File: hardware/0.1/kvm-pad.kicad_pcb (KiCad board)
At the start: 2 copper layers, 53 parts, among them J1 USB_C_Receptacle_USB2.0, J2 USB_C_Receptacle_USB2.0, J3 USB_A, J4 USB_A, J5 USB_A, U1 USBLC6-2SC6, U2 USBLC6-2SC6, U3 TS3USB30, U4 TPS211x, U5 CY7C65632-28LTXCT, Y1 12MHz

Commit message: update mask gap to 50 um
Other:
- rule pad_to_mask_clearance: 0 -> 0.05

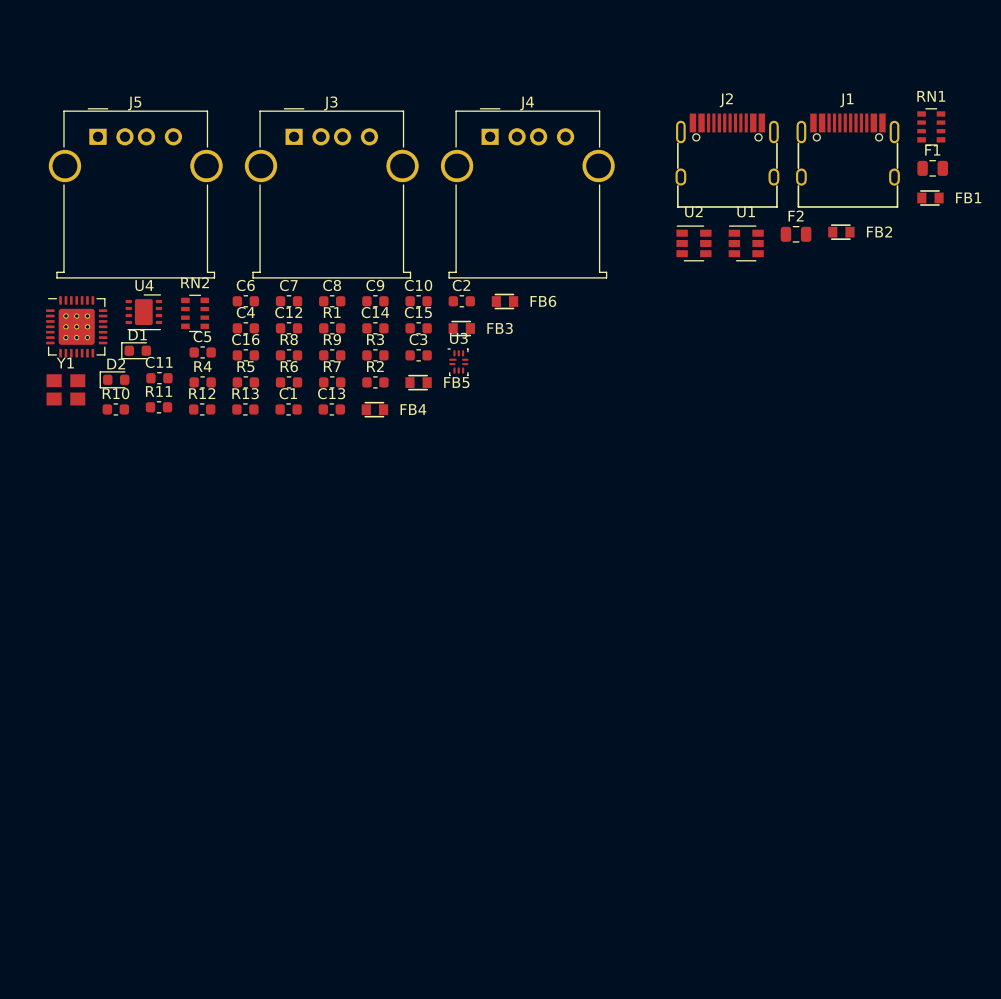
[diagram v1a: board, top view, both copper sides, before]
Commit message: Update jkl & footprints
USBA / Kailh Choc / ATMEGA32U4-AU
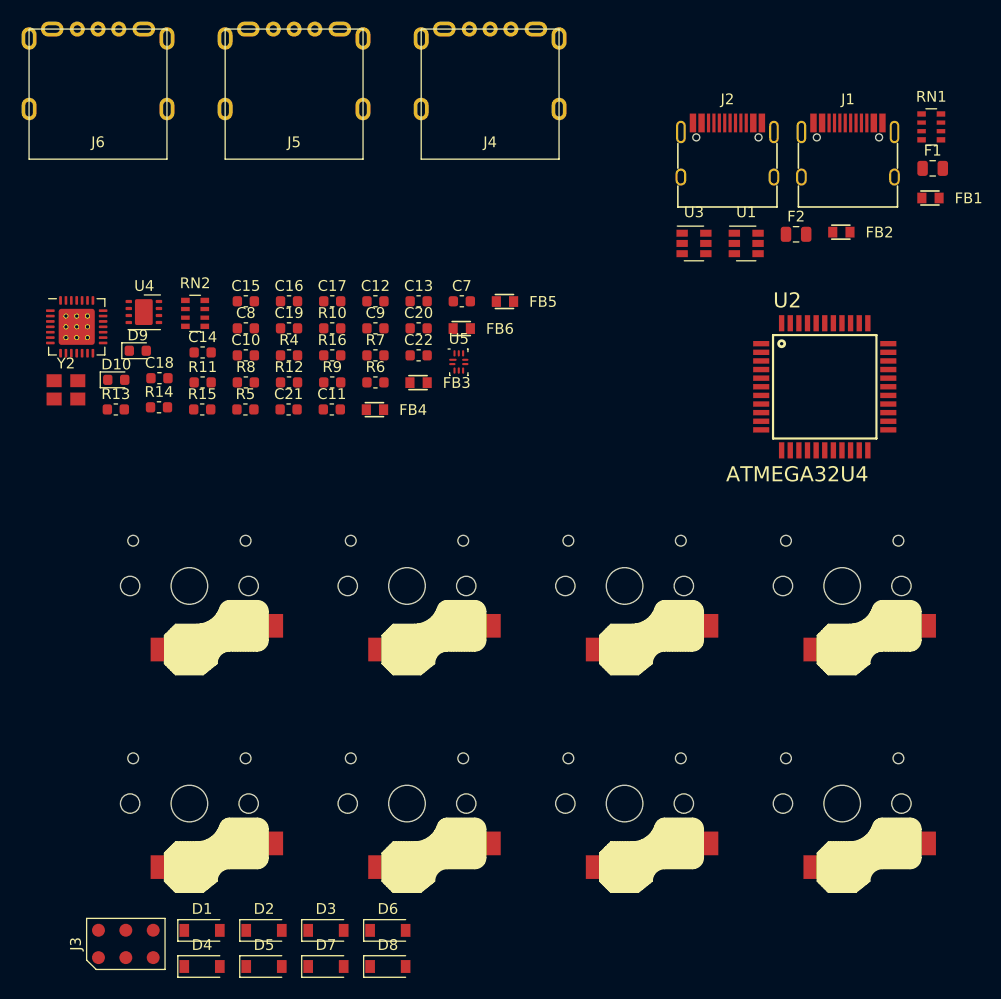
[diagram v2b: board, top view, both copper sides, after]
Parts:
- added D1: D, Diode_SMD:D_SOD-123, F.Cu at (32.4, 94.7)
- added D2: D, Diode_SMD:D_SOD-123, F.Cu at (38.1, 94.7)
- added D3: D, Diode_SMD:D_SOD-123, F.Cu at (43.9, 94.7)
- added D4: D, Diode_SMD:D_SOD-123, F.Cu at (32.4, 98.0)
- added D5: D, Diode_SMD:D_SOD-123, F.Cu at (38.1, 98.0)
- added D6: D, Diode_SMD:D_SOD-123, F.Cu at (49.6, 94.7)
- added D7: D, Diode_SMD:D_SOD-123, F.Cu at (43.9, 98.0)
- added D8: D, Diode_SMD:D_SOD-123, F.Cu at (49.6, 98.0)
- added J6: USB_A, josh-connectors:USB_A_U234-051N-3GRA035-5, F.Cu at (22.7, 21.0)
- added K1: KEYSW, josh-keyboard:Choc_Hotswap, F.Cu at (31.2, 62.7)
- added K2: KEYSW, josh-keyboard:Choc_Hotswap, F.Cu at (31.2, 82.9)
- added K3: KEYSW, josh-keyboard:Choc_Hotswap, F.Cu at (51.4, 62.7)
- added K4: KEYSW, josh-keyboard:Choc_Hotswap, F.Cu at (51.4, 82.9)
- added K5: KEYSW, josh-keyboard:Choc_Hotswap, F.Cu at (71.6, 62.7)
- added K6: KEYSW, josh-keyboard:Choc_Hotswap, F.Cu at (71.6, 82.9)
- added K7: KEYSW, josh-keyboard:Choc_Hotswap, F.Cu at (91.8, 62.7)
- added K8: KEYSW, josh-keyboard:Choc_Hotswap, F.Cu at (91.8, 82.9)
- added U2: ATMEGA32U4, josh-dfn-qfn:ATMEGA32U4-AU, F.Cu at (90.2, 44.2)
- J3: value USB_A -> AVR-ISP-6; footprint josh-connectors:USB_A_Molex_67643_Horizontal -> josh-connectors:AVR_PROG_2.54_SMT
- J4, J5: footprint josh-connectors:USB_A_Molex_67643_Horizontal -> josh-connectors:USB_A_U234-051N-3GRA035-5
- moved J3 76.5 mm to (25.3, 95.9)
- moved J5 18.2 mm to (40.9, 21.0)
- renumbered C16 to C10, C13 to C11, C9 to C12, C10 to C13, C5 to C14, C6 to C15, C7 to C16, C8 to C17, C11 to C18, C12 to C19, C15 to C20, C1 to C21, C3 to C22, C2 to C7, C4 to C8, C14 to C9, D2 to D10, D1 to D9, FB5 to FB3, FB6 to FB5, FB3 to FB6, R1 to R10, R4 to R11, R6 to R12, R10 to R13, R11 to R14, R12 to R15, R9 to R16, R8 to R4, R13 to R5, R2 to R6, R3 to R7, R5 to R8, R7 to R9, U2 to U3, U3 to U5, U5 to U6, Y1 to Y2
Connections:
- FB5 pad 1: Net-(FB6-Pad1) -> Net-(FB5-Pad1)
- J1 pad A8: (no net) -> Net-(J1-PadA8)
- J1 pad B8: (no net) -> Net-(J1-PadB8)
- J2 pad A8: (no net) -> Net-(J2-PadA8)
- J2 pad B8: (no net) -> Net-(J2-PadB8)
- J3 pad 1: Net-(FB4-Pad1) -> /MISO
- J3 pad 2: /usb/D2_D- -> +5V
- J3 pad 3: /usb/D2_D+ -> /SCK
- J3 pad 4: GND -> /MOSI
- J3 pad 5: GND -> /nRST
- J5 pad 1: Net-(FB6-Pad1) -> Net-(FB4-Pad1)
- J5 pad 2: /usb/D3_D- -> /usb/D2_D-
- J5 pad 3: /usb/D3_D+ -> /usb/D2_D+
- R10 pad 2: (no net) -> /SWITCH
- U6 pad 15: (no net) -> /MCU_D-
- U6 pad 16: (no net) -> /MCU_D+
- U6 pad 18: (no net) -> Net-(U6-Pad18)
- U6 pad 26: (no net) -> Net-(U6-Pad26)

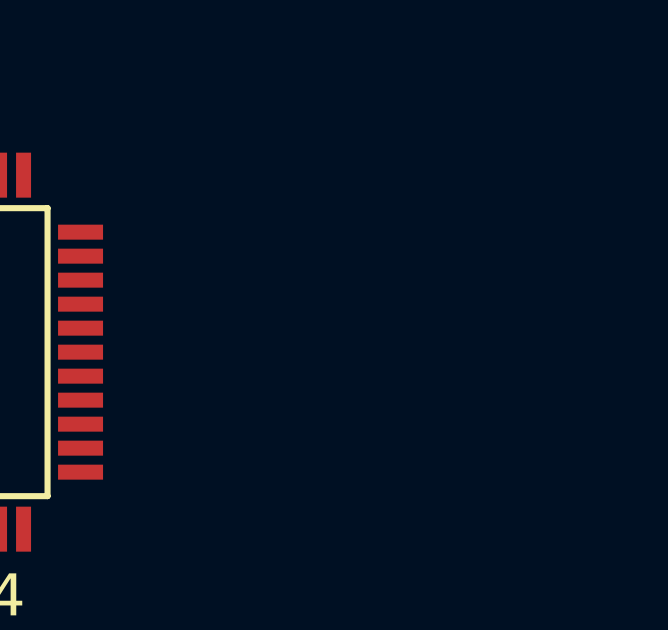
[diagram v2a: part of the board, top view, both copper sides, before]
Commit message: Add missing footprints
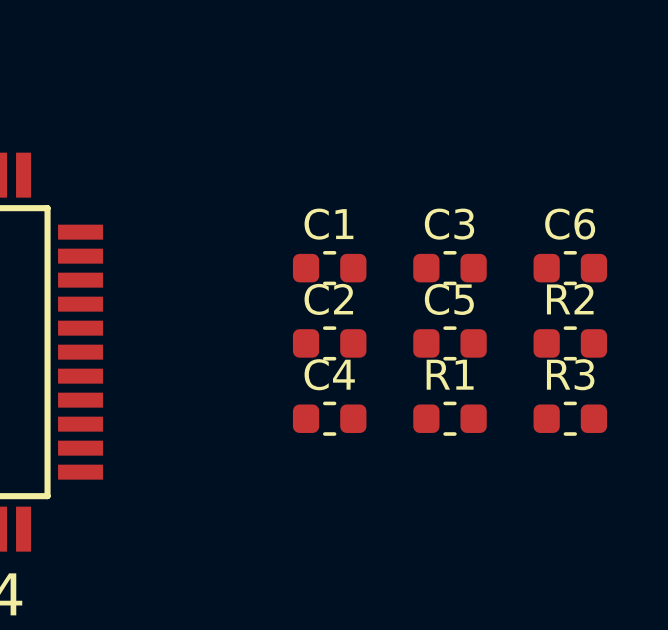
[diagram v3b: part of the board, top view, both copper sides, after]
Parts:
- added C1: 1u, Capacitor_SMD:C_0603_1608Metric, F.Cu at (104.4, 41.4)
- added C2: 100n, Capacitor_SMD:C_0603_1608Metric, F.Cu at (104.4, 43.9)
- added C3: 100n, Capacitor_SMD:C_0603_1608Metric, F.Cu at (108.4, 41.4)
- added C4: 22p, Capacitor_SMD:C_0603_1608Metric, F.Cu at (104.4, 46.4)
- added C5: 22p, Capacitor_SMD:C_0603_1608Metric, F.Cu at (108.4, 43.9)
- added C6: 1u, Capacitor_SMD:C_0603_1608Metric, F.Cu at (112.4, 41.4)
- added R1: 22R, Resistor_SMD:R_0603_1608Metric, F.Cu at (108.4, 46.4)
- added R2: 22R, Resistor_SMD:R_0603_1608Metric, F.Cu at (112.4, 43.9)
- added R3: 10K, Resistor_SMD:R_0603_1608Metric, F.Cu at (112.4, 46.4)

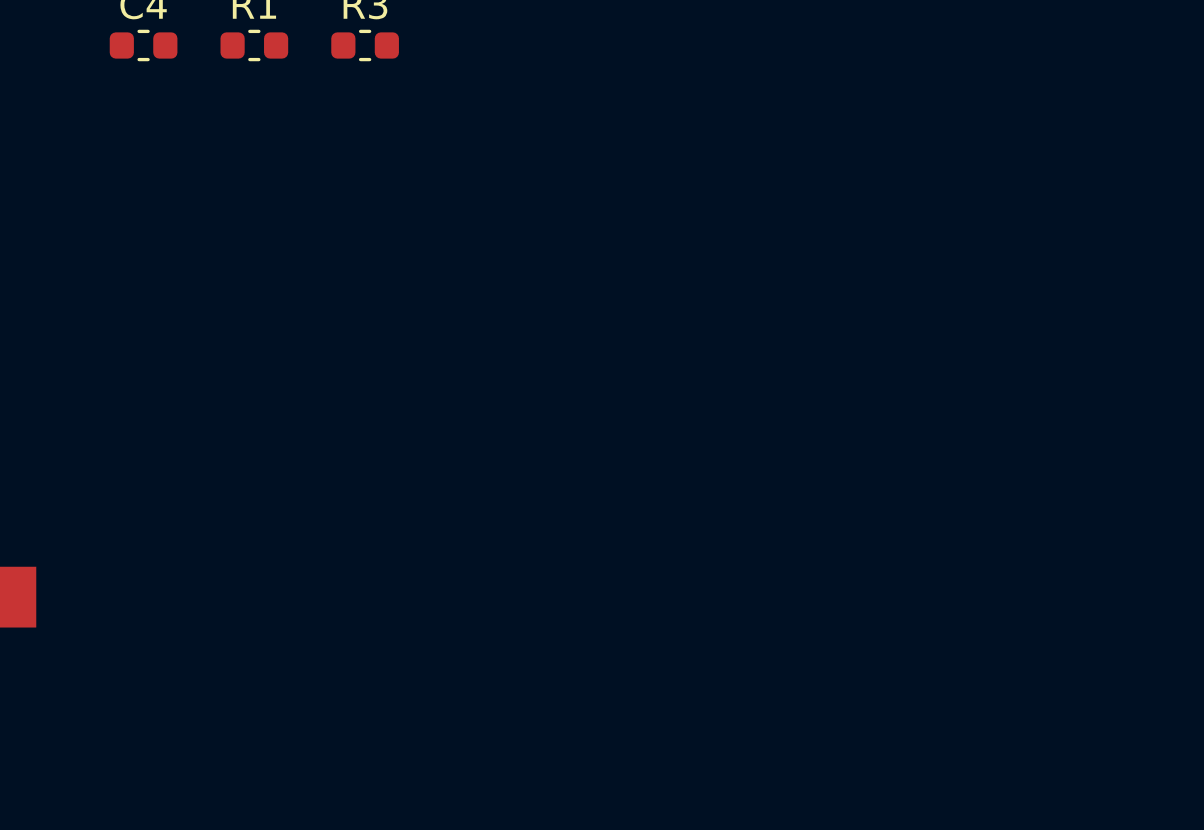
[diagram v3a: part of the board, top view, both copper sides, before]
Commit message: Add RGB LEDs
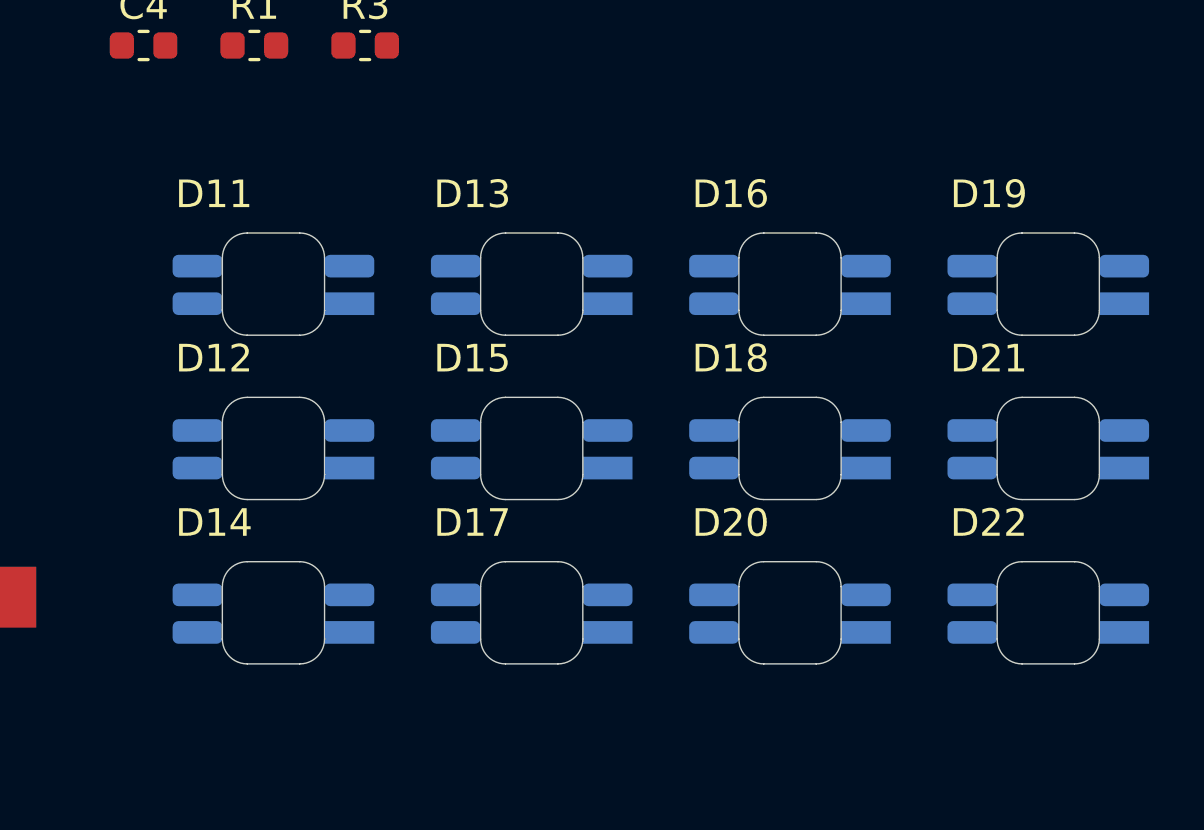
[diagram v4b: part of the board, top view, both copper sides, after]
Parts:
- added D11: WS2812B, josh-led:SK8612-MINI-E, F.Cu at (109.0, 55.1)
- added D12: WS2812B, josh-led:SK8612-MINI-E, F.Cu at (109.0, 61.1)
- added D13: WS2812B, josh-led:SK8612-MINI-E, F.Cu at (118.4, 55.1)
- added D14: WS2812B, josh-led:SK8612-MINI-E, F.Cu at (109.0, 67.0)
- added D15: WS2812B, josh-led:SK8612-MINI-E, F.Cu at (118.4, 61.1)
- added D16: WS2812B, josh-led:SK8612-MINI-E, F.Cu at (127.7, 55.1)
- added D17: WS2812B, josh-led:SK8612-MINI-E, F.Cu at (118.4, 67.0)
- added D18: WS2812B, josh-led:SK8612-MINI-E, F.Cu at (127.7, 61.1)
- added D19: WS2812B, josh-led:SK8612-MINI-E, F.Cu at (137.1, 55.1)
- added D20: WS2812B, josh-led:SK8612-MINI-E, F.Cu at (127.7, 67.0)
- added D21: WS2812B, josh-led:SK8612-MINI-E, F.Cu at (137.1, 61.1)
- added D22: WS2812B, josh-led:SK8612-MINI-E, F.Cu at (137.1, 67.0)
- moved LOGO1 108.0 mm to (102.9, 100.6)
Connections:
- U2 pad 18: /col1 -> Net-(U2-Pad18)
- U2 pad 19: /col2 -> /LED_DAT
- U2 pad 20: /col3 -> /col1
- U2 pad 21: /col4 -> /col2
- U2 pad 22: Net-(U2-Pad22) -> /col4
- U2 pad 25: Net-(U2-Pad25) -> /col3
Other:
- board outline added: 3.7 x 3.7 mm

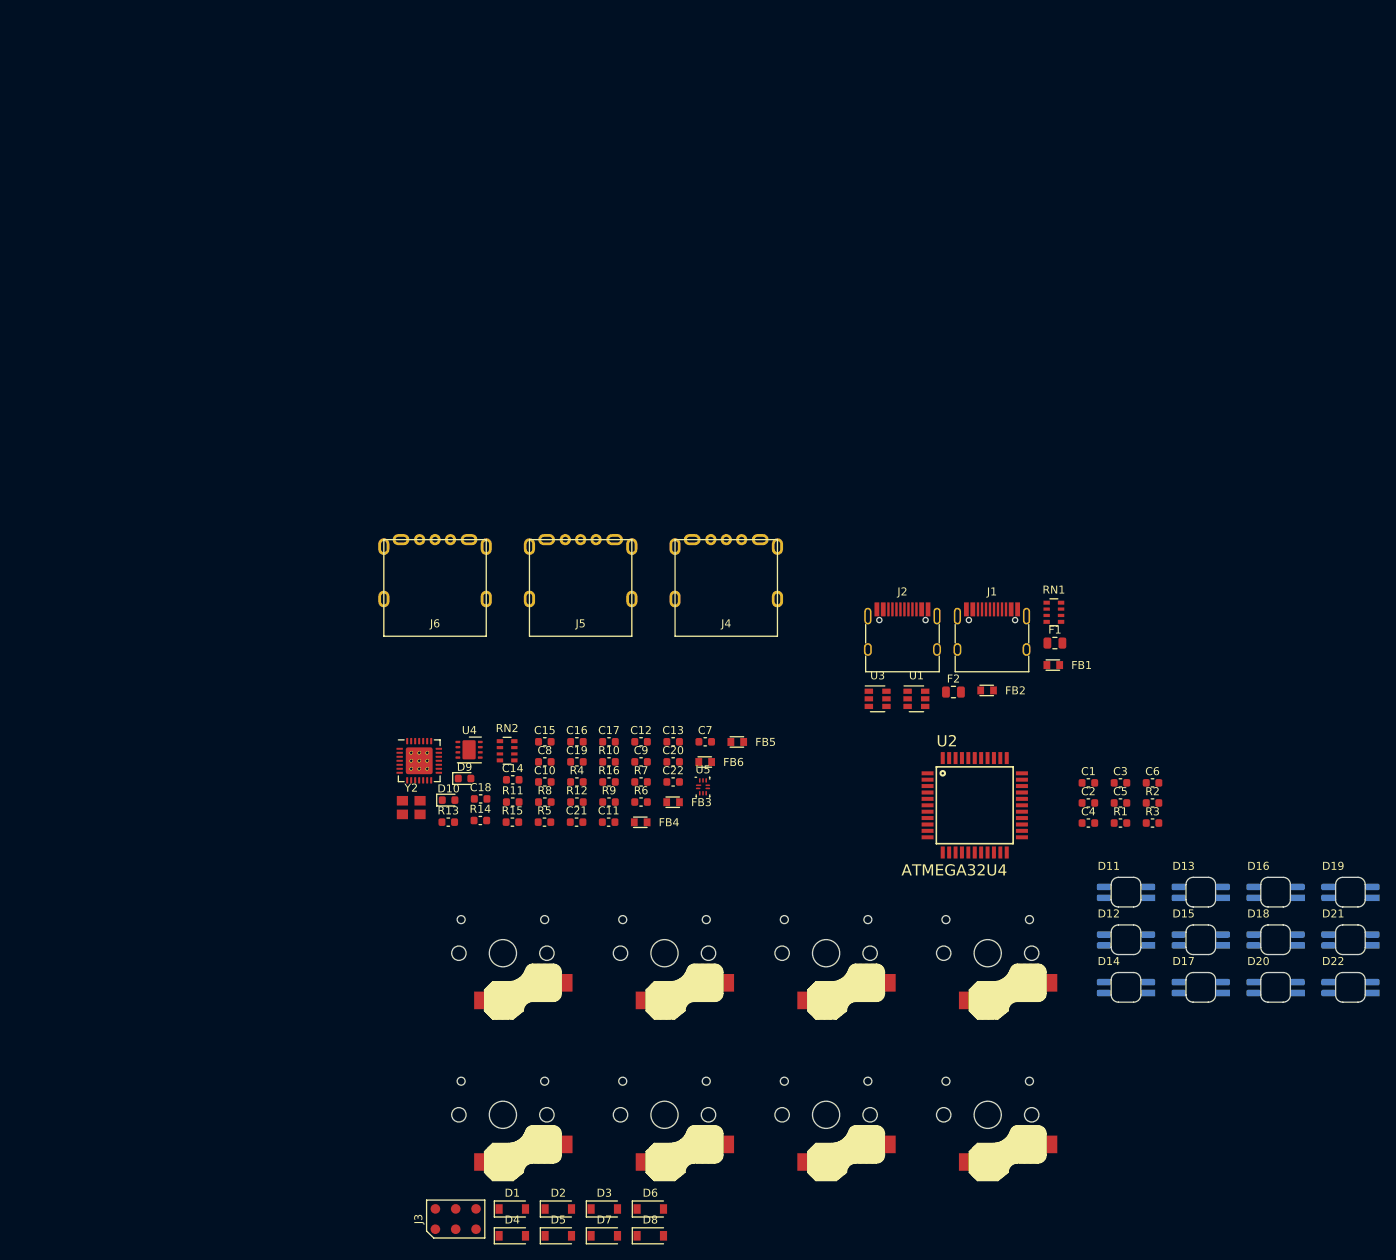
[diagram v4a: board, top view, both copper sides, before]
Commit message: WIP PCB Layout with parts grouped
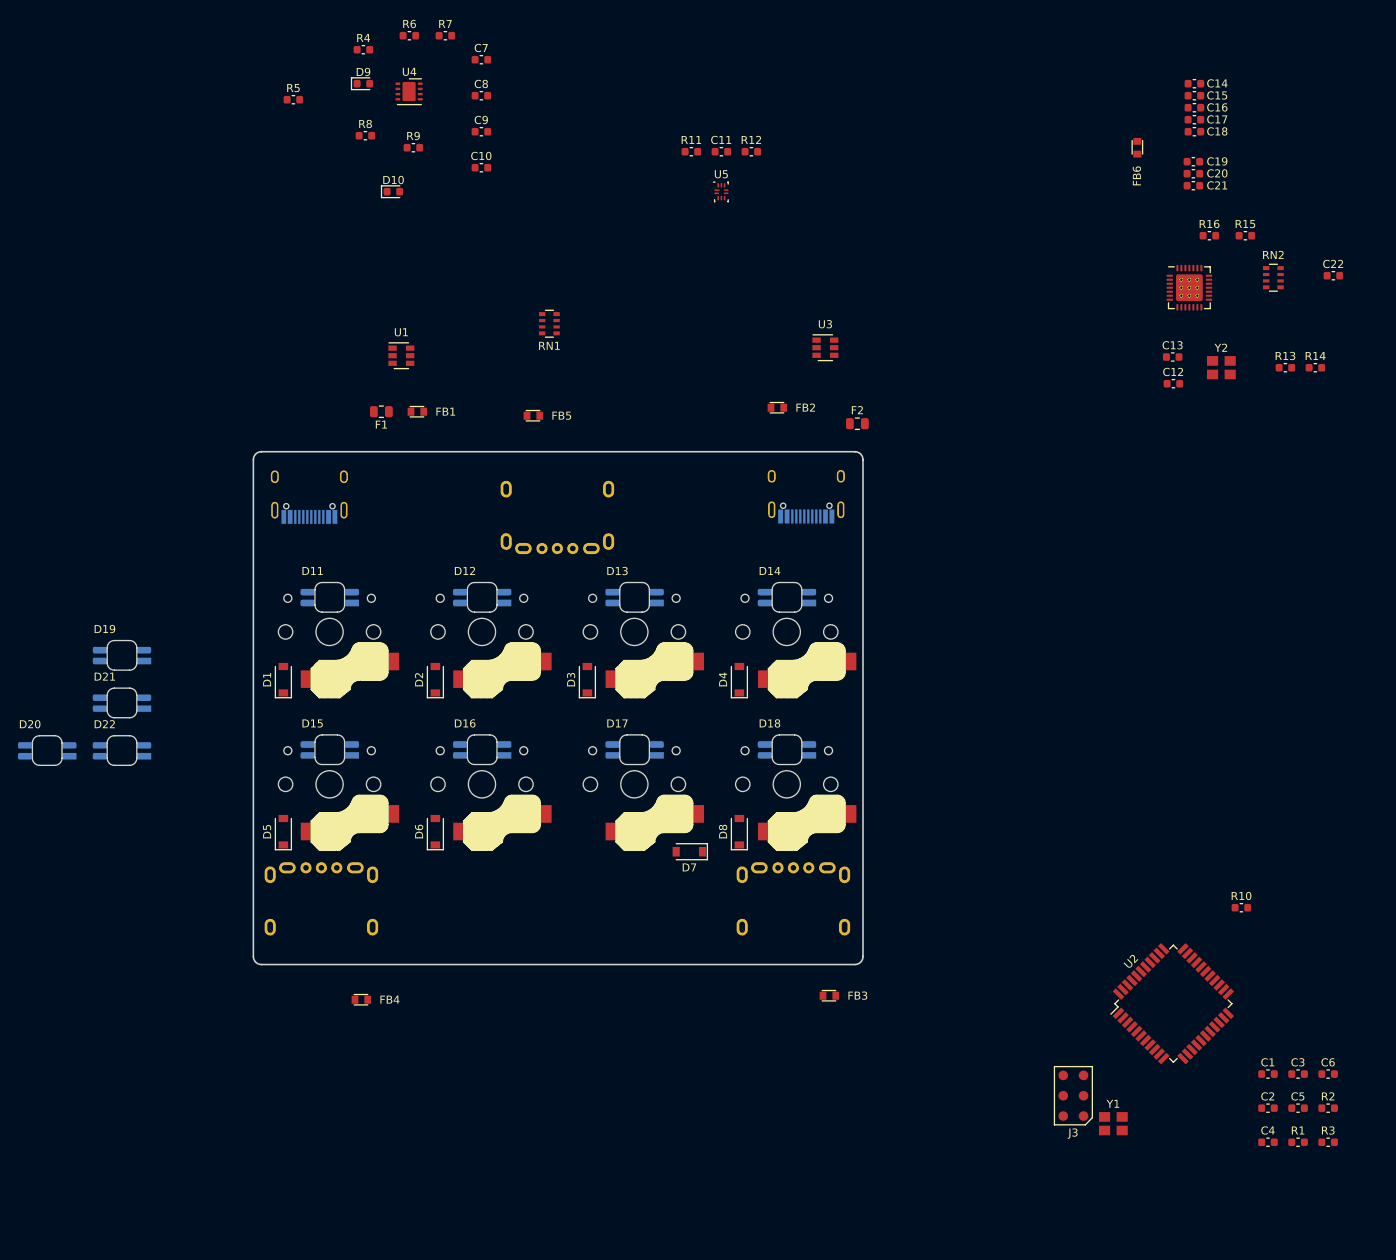
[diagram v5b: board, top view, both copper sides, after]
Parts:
- added Y1: 16MHz, josh-oscillators:Crystal_SMD_3225-4Pin_3.2x2.5mm, F.Cu at (107.5, 84.0)
- J1, J2, J4, J5, J6: moved to B.Cu
- U2: footprint josh-dfn-qfn:ATMEGA32U4-AU -> Package_QFP:TQFP-44_10x10mm_P0.8mm
- moved D19 156.4 mm to (-16.5, 25.5)
- moved D20 156.4 mm to (-25.8, 37.4)
- moved D21 156.4 mm to (-16.5, 31.5)
- moved D22 156.4 mm to (-16.5, 37.4)
- moved C18 122.1 mm to (117.6, -40.0)
- moved C14 121.8 mm to (117.6, -46.0)
- moved R13 119.1 mm to (129.0, -10.5)
- moved R14 118.7 mm to (132.8, -10.5)
- moved R15 117.3 mm to (124.0, -27.0)
- moved Y2 115.2 mm to (121.0, -10.5)
- moved C15 114.5 mm to (117.6, -44.5)
- moved U6 113.0 mm to (117.0, -20.5)
- moved RN2 112.6 mm to (127.5, -21.8)
- moved D15 111.4 mm to (9.50, 37.3)
- moved C21 110.8 mm to (117.5, -33.2)
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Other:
- board size 3.7 x 3.7 mm -> 76.2 x 64.1 mm
